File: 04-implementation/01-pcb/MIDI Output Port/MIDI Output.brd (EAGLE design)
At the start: 102.9 x 29.8 mm, 34 parts, among them IC1 741G32, IC2 741G32, IC3 741G32, IC4 741G32, J1 SSW-107-02-S-D, U1 SDS-50J, U2 SDS-50J, U3 SDS-50J, U4 SDS-50J

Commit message: Revise MIDI PCB's for mechanical spacing of ribbon connector.
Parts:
- removed C1, C3, C5, C7, C9: 100n, rcl:C0805
- moved J1 2.99 mm to (99.7, 9.78)
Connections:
- removed net N$10: C3.1, U2.P$6, U2.P$7
- removed net N$19: C5.1, U3.P$6, U3.P$7
- removed net N$27: C7.1, U4.P$6, U4.P$7
- removed net N$6: C1.1, U1.P$6, U1.P$7
- net +5V: no longer C9.1
- net GND: now also U1.P$6, U1.P$7, U2.P$6, U2.P$7, U3.P$6, U3.P$7, U4.P$6, U4.P$7; no longer C1.2, C3.2, C5.2, C7.2, C9.2
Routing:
- net GND: track 0.00 -> 22.5 mm
- net N$6: track 6.46 -> 0.00 mm
- net N$27: track 6.46 -> 0.00 mm
- net N$10: track 6.46 -> 0.00 mm
- net N$19: track 6.46 -> 0.00 mm
- net D-OUT3: track 56.9 -> 53.5 mm
- net D-OUT4: track 36.7 -> 34.1 mm
- net D-OUT2: track 77.9 -> 75.5 mm
- net +5V: track 29.7 -> 27.7 mm, vias 9 -> 8
- net D-OUT1: track 98.9 -> 98.4 mm
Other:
- board text added: "HW 0004"
- board text removed: "HW 0003"

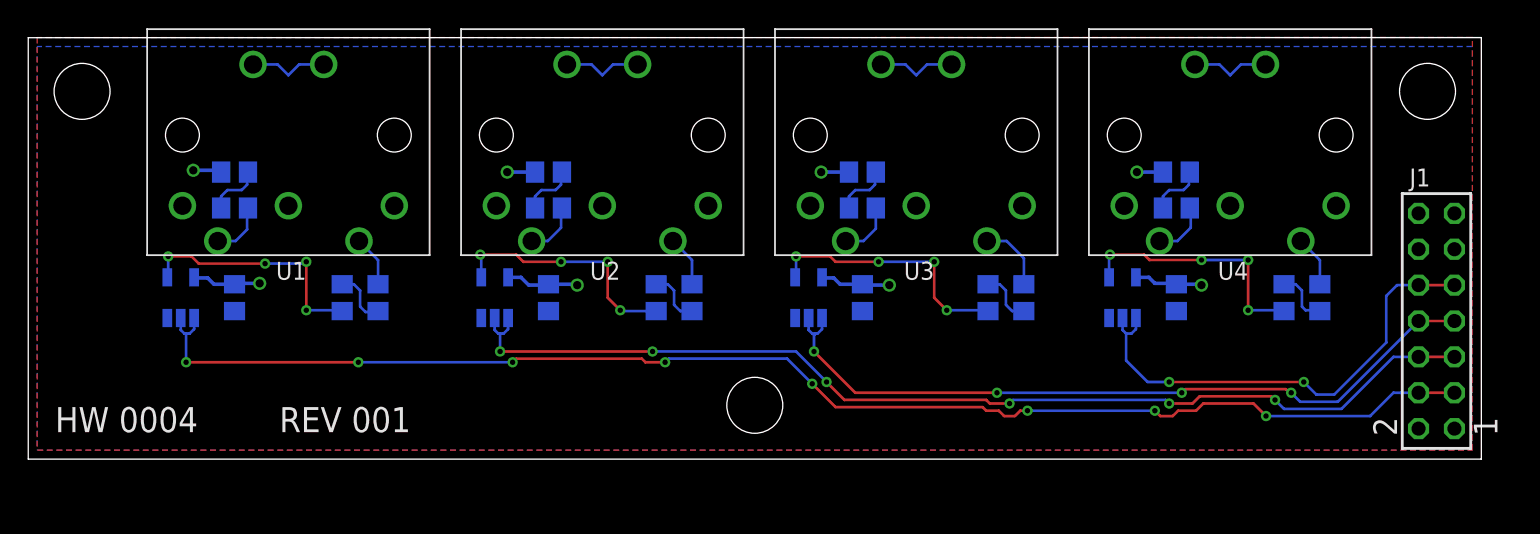
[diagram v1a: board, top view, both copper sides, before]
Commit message: Add files for PCB releases.
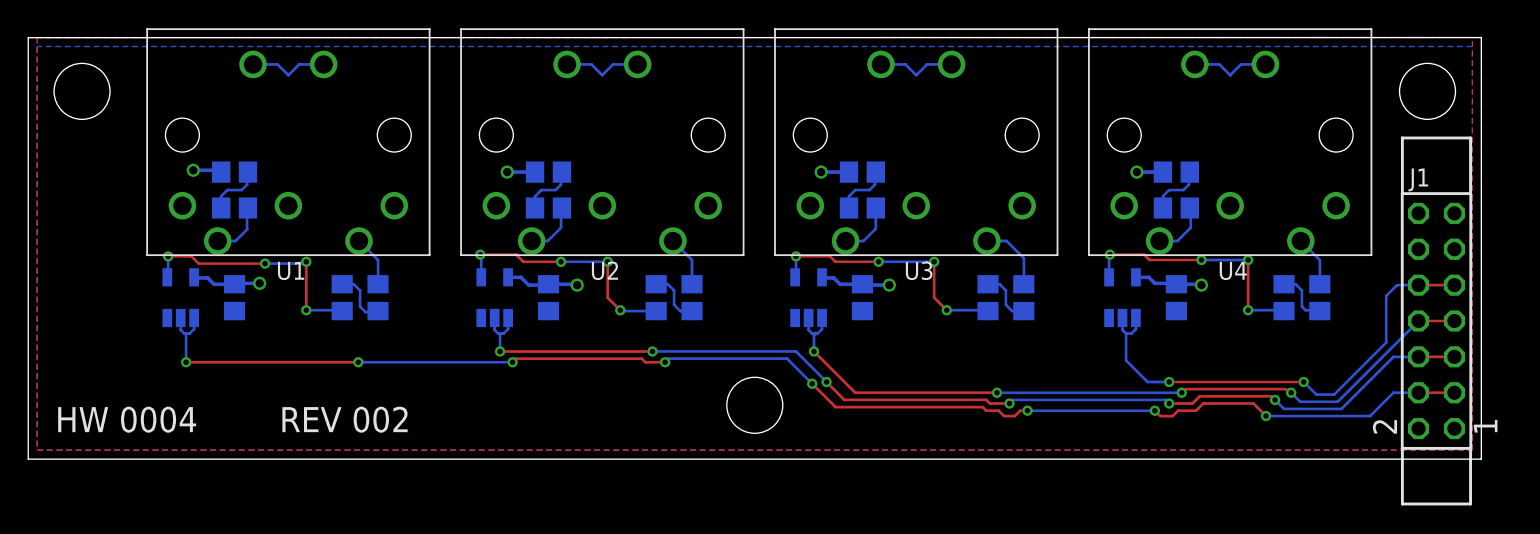
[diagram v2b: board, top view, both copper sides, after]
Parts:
- J1: value SSW-107-02-S-D -> SSW-107-02-G-D; device con-samtec:SSW-107-02-S-D -> MIDI router parts:SSW-107-02-G-D
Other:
- board text added: "REV 002"
- board text removed: "REV 001"
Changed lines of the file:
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@@
 <?xml version="1.0" encoding="utf-8"?>
 <!DOCTYPE eagle SYSTEM "eagle.dtd">
-<eagle version="9.0.1">
+<eagle version="9.3.0">
 <drawing>
 <settings>
@@
 <layer number="51" name="tDocu" color="7" fill="1" visible="yes" active="yes"/>
 <layer number="52" name="bDocu" color="7" fill="1" visible="yes" active="yes"/>
+<layer number="88" name="SimResults" color="9" fill="1" visible="no" active="no"/>
+<layer number="89" name="SimProbes" color="9" fill="1" visible="no" active="no"/>
 <layer number="90" name="Modules" color="5" fill="1" visible="no" active="no"/>
 <layer number="91" name="Nets" color="2" fill="1" visible="no" active="no"/>
@@
 <hole x="51.435" y="3.81" drill="3.9624"/>
 <text x="1.905" y="1.905" size="1.778" layer="25">HW 0004</text>
-<text x="17.78" y="1.905" size="1.778" layer="25">REV 001</text>
+<text x="17.78" y="1.905" size="1.778" layer="25">REV 002</text>
 </plain>
 <attributes>
@@
 <param name="checkStop" value="0"/>
 <param name="checkValues" value="0"/>
+<param name="checkNames" value="1"/>
+<param name="checkWireStubs" value="1"/>
+<param name="checkPolygonWidth" value="0"/>
 <param name="useDiameter" value="13"/>
 <param name="maxErrors" value="50"/>
@@
 <element name="R1" library="rcl" library_urn="urn:adsk.eagle:library:334" package="R0805" package3d_urn="urn:adsk.eagle:package:23553/2" value="220" x="22.225" y="11.43" smashed="yes" rot="MR90">
 <attribute name="NAME" x="22.86" y="9.525" size="1.27" layer="26" rot="MR270"/>
+<attribute name="SPICEPREFIX" value="R" x="22.225" y="11.43" size="1.778" layer="28" rot="MR90" display="off"/>
 <attribute name="VALUE" x="19.685" y="10.795" size="1.27" layer="28" rot="MR90"/>
 </element>
-<element name="J1" library="con-samtec" library_urn="urn:adsk.eagle:library:184" package="SSW-107-02-S-D" value="SSW-107-02-S-D" x="99.695" y="9.779" smashed="yes" rot="R90">
-<attribute name="MF" value="" x="99.695" y="9.779" size="1.778" layer="27" rot="R90" display="off"/>
-<attribute name="MPN" value="SSW-107-02-S-D" x="99.695" y="9.779" size="1.778" layer="27" rot="R90" display="off"/>
+<element name="J1" library="MIDI router parts" package="SSW-107-02-G-D" value="SSW-107-02-G-D" x="99.695" y="9.779" smashed="yes" rot="R90">
+<attribute name="MF" value="Samtec Inc." x="99.695" y="9.779" size="1.778" layer="27" rot="R90" display="off"/>
+<attribute name="MPN" value="SSW-107-02-G-D" x="99.695" y="9.779" size="1.778" layer="27" rot="R90" display="off"/>
 <attribute name="NAME" x="97.79" y="19.304" size="1.27" layer="25"/>
 <attribute name="OC_FARNELL" value="unknown" x="99.695" y="9.779" size="1.778" layer="27" rot="R90" display="off"/>
@@
 <element name="R2" library="rcl" library_urn="urn:adsk.eagle:library:334" package="R0805" package3d_urn="urn:adsk.eagle:package:23553/2" value="220" x="14.605" y="17.78" smashed="yes" rot="MR0">
 <attribute name="NAME" x="15.24" y="16.51" size="1.27" layer="26" rot="MR180"/>
+<attribute name="SPICEPREFIX" value="R" x="14.605" y="17.78" size="1.778" layer="28" rot="MR0" display="off"/>
 <attribute name="VALUE" x="15.24" y="15.24" size="1.27" layer="28" rot="MR0"/>
 </element>
 <element name="C2" library="rcl" library_urn="urn:adsk.eagle:library:334" package="C0805" package3d_urn="urn:adsk.eagle:package:23617/2" value="100n" x="14.605" y="11.43" smashed="yes" rot="MR270">
 <attribute name="NAME" x="15.24" y="9.525" size="1.27" layer="26" rot="MR270"/>
+<attribute name="SPICEPREFIX" value="C" x="14.605" y="11.43" size="1.778" layer="28" rot="MR270" display="off"/>
 <attribute name="VALUE" x="17.145" y="12.7" size="1.27" layer="28" rot="MR270"/>
 </element>
@@
 <element name="R3" library="rcl" library_urn="urn:adsk.eagle:library:334" package="R0805" package3d_urn="urn:adsk.eagle:package:23553/2" value="220" x="44.45" y="11.43" smashed="yes" rot="MR90">
 <attribute name="NAME" x="45.085" y="9.525" size="1.27" layer="26" rot="MR270"/>
+<attribute name="SPICEPREFIX" value="R" x="44.45" y="11.43" size="1.778" layer="28" rot="MR90" display="off"/>
 <attribute name="VALUE" x="41.91" y="10.795" size="1.27" layer="28" rot="MR90"/>
 </element>
@@
 <element name="R4" library="rcl" library_urn="urn:adsk.eagle:library:334" package="R0805" package3d_urn="urn:adsk.eagle:package:23553/2" value="220" x="36.83" y="17.78" smashed="yes" rot="MR0">
 <attribute name="NAME" x="37.465" y="16.51" size="1.27" layer="26" rot="MR180"/>
+<attribute name="SPICEPREFIX" value="R" x="36.83" y="17.78" size="1.778" layer="28" rot="MR0" display="off"/>
 <attribute name="VALUE" x="37.465" y="15.24" size="1.27" layer="28" rot="MR0"/>
 </element>
 <element name="C4" library="rcl" library_urn="urn:adsk.eagle:library:334" package="C0805" package3d_urn="urn:adsk.eagle:package:23617/2" value="100n" x="36.83" y="11.43" smashed="yes" rot="MR270">
 <attribute name="NAME" x="37.465" y="9.525" size="1.27" layer="26" rot="MR270"/>
+<attribute name="SPICEPREFIX" value="C" x="36.83" y="11.43" size="1.778" layer="28" rot="MR270" display="off"/>
 <attribute name="VALUE" x="39.37" y="12.7" size="1.27" layer="28" rot="MR270"/>
 </element>
@@
 <element name="R5" library="rcl" library_urn="urn:adsk.eagle:library:334" package="R0805" package3d_urn="urn:adsk.eagle:package:23553/2" value="220" x="67.945" y="11.43" smashed="yes" rot="MR90">
 <attribute name="NAME" x="68.58" y="9.525" size="1.27" layer="26" rot="MR270"/>
+<attribute name="SPICEPREFIX" value="R" x="67.945" y="11.43" size="1.778" layer="28" rot="MR90" display="off"/>
 <attribute name="VALUE" x="65.405" y="10.795" size="1.27" layer="28" rot="MR90"/>
 </element>
@@
 <element name="R6" library="rcl" library_urn="urn:adsk.eagle:library:334" package="R0805" package3d_urn="urn:adsk.eagle:package:23553/2" value="220" x="59.055" y="17.78" smashed="yes" rot="MR0">
 <attribute name="NAME" x="59.69" y="16.51" size="1.27" layer="26" rot="MR180"/>
+<attribute name="SPICEPREFIX" value="R" x="59.055" y="17.78" size="1.778" layer="28" rot="MR0" display="off"/>
 <attribute name="VALUE" x="59.69" y="15.24" size="1.27" layer="28" rot="MR0"/>
 </element>
 <element name="C6" library="rcl" library_urn="urn:adsk.eagle:library:334" package="C0805" package3d_urn="urn:adsk.eagle:package:23617/2" value="100n" x="59.055" y="11.43" smashed="yes" rot="MR270">
 <attribute name="NAME" x="59.69" y="9.525" size="1.27" layer="26" rot="MR270"/>
+<attribute name="SPICEPREFIX" value="C" x="59.055" y="11.43" size="1.778" layer="28" rot="MR270" display="off"/>
 <attribute name="VALUE" x="61.595" y="12.7" size="1.27" layer="28" rot="MR270"/>
 </element>
@@
 <element name="R7" library="rcl" library_urn="urn:adsk.eagle:library:334" package="R0805" package3d_urn="urn:adsk.eagle:package:23553/2" value="220" x="88.9" y="11.43" smashed="yes" rot="MR90">
 <attribute name="NAME" x="89.535" y="9.525" size="1.27" layer="26" rot="MR270"/>
+<attribute name="SPICEPREFIX" value="R" x="88.9" y="11.43" size="1.778" layer="28" rot="MR90" display="off"/>
 <attribute name="VALUE" x="86.36" y="10.795" size="1.27" layer="28" rot="MR90"/>
 </element>
@@
 <element name="R8" library="rcl" library_urn="urn:adsk.eagle:library:334" package="R0805" package3d_urn="urn:adsk.eagle:package:23553/2" value="220" x="81.28" y="17.78" smashed="yes" rot="MR0">
 <attribute name="NAME" x="81.915" y="16.51" size="1.27" layer="26" rot="MR180"/>
+<attribute name="SPICEPREFIX" value="R" x="81.28" y="17.78" size="1.778" layer="28" rot="MR0" display="off"/>
 <attribute name="VALUE" x="81.915" y="15.24" size="1.27" layer="28" rot="MR0"/>
 </element>
 <element name="C8" library="rcl" library_urn="urn:adsk.eagle:library:334" package="C0805" package3d_urn="urn:adsk.eagle:package:23617/2" value="100n" x="81.28" y="11.43" smashed="yes" rot="MR270">
 <attribute name="NAME" x="81.915" y="9.525" size="1.27" layer="26" rot="MR270"/>
+<attribute name="SPICEPREFIX" value="C" x="81.28" y="11.43" size="1.778" layer="28" rot="MR270" display="off"/>
 <attribute name="VALUE" x="83.82" y="12.7" size="1.27" layer="28" rot="MR270"/>
 </element>
@@
 </signal>
 </signals>
+<mfgpreviewcolors>
+<mfgpreviewcolor name="soldermaskcolor" color="0xC8008000"/>
+<mfgpreviewcolor name="silkscreencolor" color="0xFFFEFEFE"/>
+<mfgpreviewcolor name="backgroundcolor" color="0xFF282828"/>
+<mfgpreviewcolor name="coppercolor" color="0xFFFFBF00"/>
+<mfgpreviewcolor name="substratecolor" color="0xFF786E46"/>
+</mfgpreviewcolors>
 </board>
 </drawing>
